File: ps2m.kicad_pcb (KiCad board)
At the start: 2 copper layers, 6 parts, among them P1 MOUSE_PORT, P2 MINI_DIN_6, U1 PIC16(L)F627-xxI/SS

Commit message: Imperial drill file for Seeed
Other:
- board text added: "Mounting holes for DB9 must be removed from gerber plot."
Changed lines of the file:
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@@
 (kicad_pcb (version 4) (host pcbnew 4.0.5)
   (general
-    (links 0)
+    (links 23)
     (no_connects 0)
     (area 134.724999 78.224999 167.275001 115.775)
     (thickness 1.6)
-    (drawings 37)
+    (drawings 40)
     (tracks 151)
     (zones 0)
@@
       (net 9 /MOUSE_9))
   )
+  (gr_text "Mounting holes for\nDB9 must be removed\nfrom gerber plot." (at 177.5 87.5) (layer Cmts.User)
+    (effects (font (size 1.5 1.5) (thickness 0.3)) (justify left))
+  )
+  (dimension 14 (width 0.3) (layer Cmts.User)
+    (gr_text "14.000 mm" (at 151 117.85) (layer Cmts.User)
+      (effects (font (size 1.5 1.5) (thickness 0.3)))
+    )
+    (feature1 (pts (xy 158 114) (xy 158 119.2)))
+    (feature2 (pts (xy 144 114) (xy 144 119.2)))
+    (crossbar (pts (xy 144 116.5) (xy 158 116.5)))
+    (arrow1a (pts (xy 158 116.5) (xy 156.873496 117.086421)))
+    (arrow1b (pts (xy 158 116.5) (xy 156.873496 115.913579)))
+    (arrow2a (pts (xy 144 116.5) (xy 145.126504 117.086421)))
+    (arrow2b (pts (xy 144 116.5) (xy 145.126504 115.913579)))
+  )
+  (dimension 28 (width 0.3) (layer Cmts.User)
+    (gr_text "28.000 mm" (at 171.6 99.5 270) (layer Cmts.User)
+      (effects (font (size 1.5 1.5) (thickness 0.3)))
+    )
+    (feature1 (pts (xy 167.5 113.5) (xy 172.95 113.5)))
+    (feature2 (pts (xy 167.5 85.5) (xy 172.95 85.5)))
+    (crossbar (pts (xy 170.25 85.5) (xy 170.25 113.5)))
+    (arrow1a (pts (xy 170.25 113.5) (xy 169.663579 112.373496)))
+    (arrow1b (pts (xy 170.25 113.5) (xy 170.836421 112.373496)))
+    (arrow2a (pts (xy 170.25 85.5) (xy 169.663579 86.626504)))
+    (arrow2b (pts (xy 170.25 85.5) (xy 170.836421 86.626504)))
+  )
   (gr_arc (start 157.25 86.25) (end 157.25 85.5) (angle 90) (layer Margin) (width 0.2))

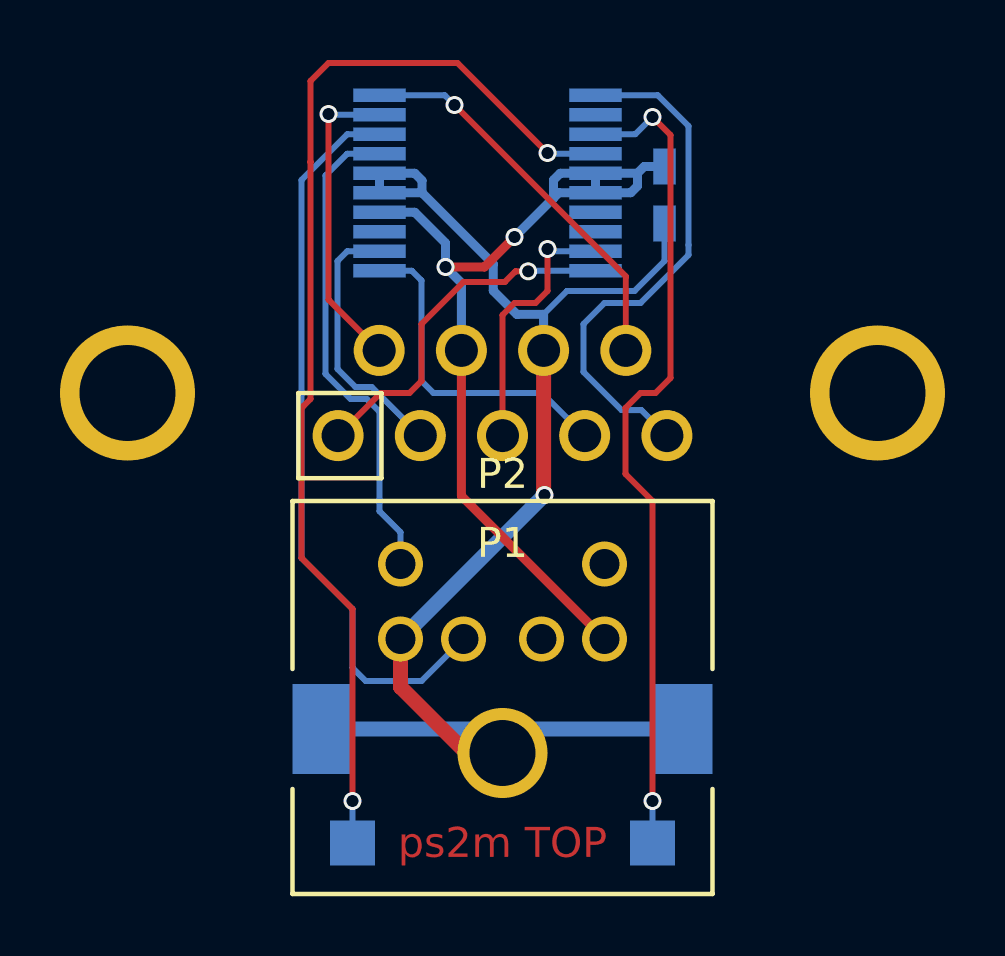
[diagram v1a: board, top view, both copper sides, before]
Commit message: Fixed MiniDIN footprint and narrowed board to accomodate
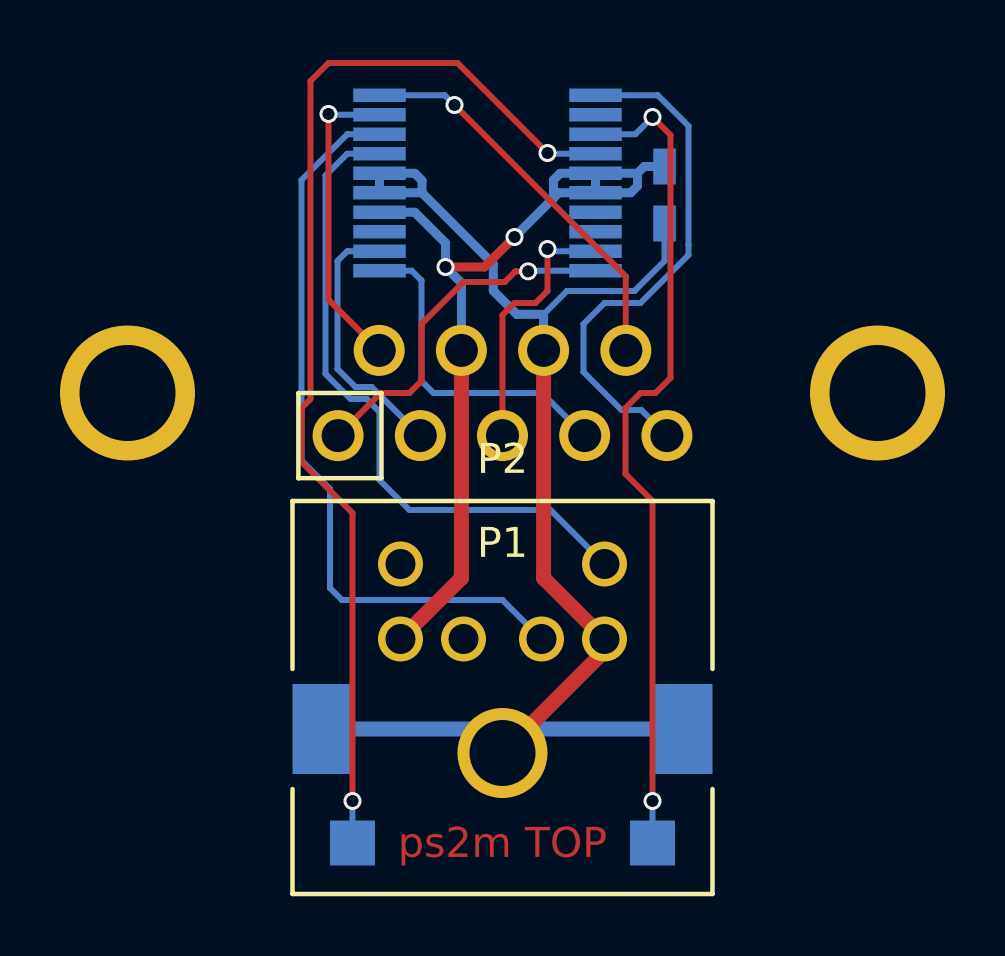
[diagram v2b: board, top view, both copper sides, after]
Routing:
- net /MINIDIN_5: track 16.4 -> 22.0 mm
- net GND: track 47.7 -> 45.8 mm, vias 1 -> 0
- net +5V: track 31.1 -> 30.0 mm

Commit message: V1.1 improved tracking/placement
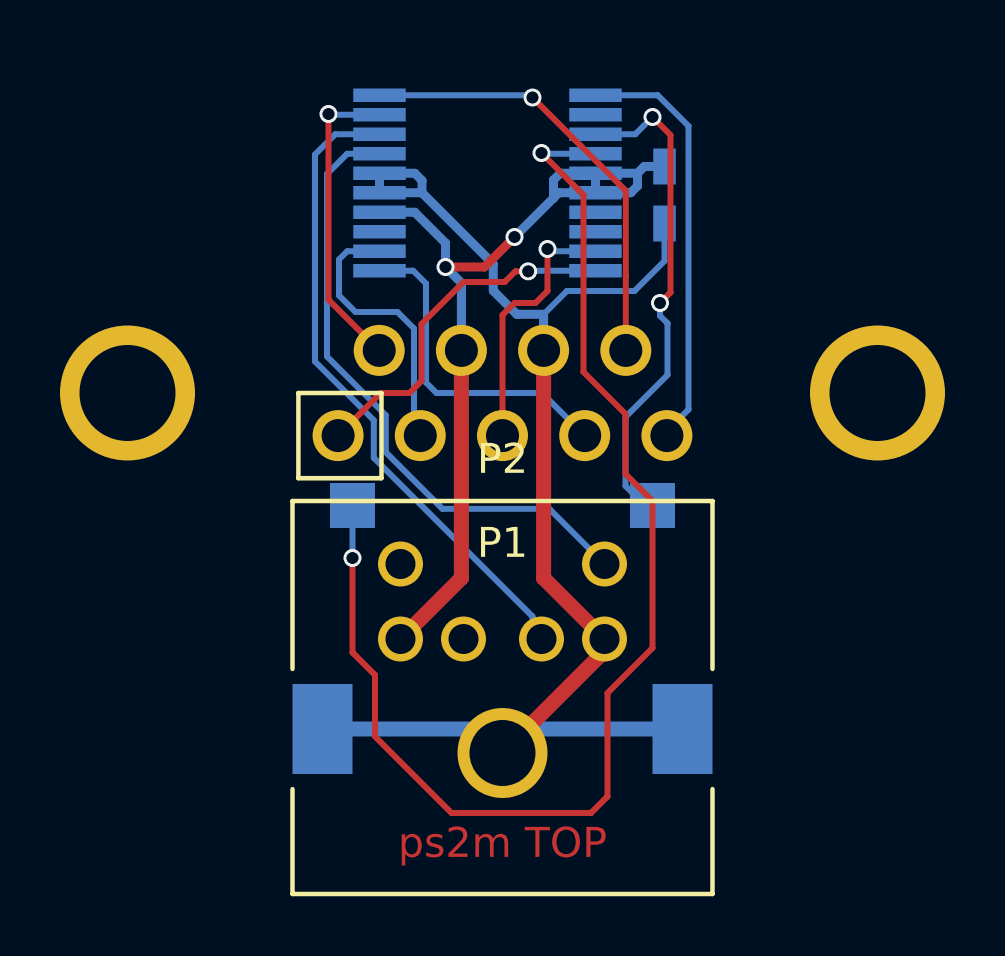
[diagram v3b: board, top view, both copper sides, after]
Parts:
- moved W1 11.2 mm to (146.0, 100.8)
- moved W3 11.2 mm to (156.0, 100.8)
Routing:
- net /JOY_3: track 27.9 -> 16.7 mm
- net /JOY_1: track 37.2 -> 42.5 mm
- net /MOUSE_5: track 17.5 -> 14.1 mm
- net /MINIDIN_1: track 25.0 -> 21.7 mm
- net /MOUSE_9: track 13.8 -> 15.5 mm
- net /MINIDIN_5: track 22.0 -> 20.9 mm
